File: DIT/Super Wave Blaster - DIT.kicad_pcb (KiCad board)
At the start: 2 copper layers, 28.2 x 21.2 mm, 20 parts, among them J1 SPDIF, J4 Power Input, U1 TLV73333PDBV, U2 DIT4096PW, U4 74LVC2G125

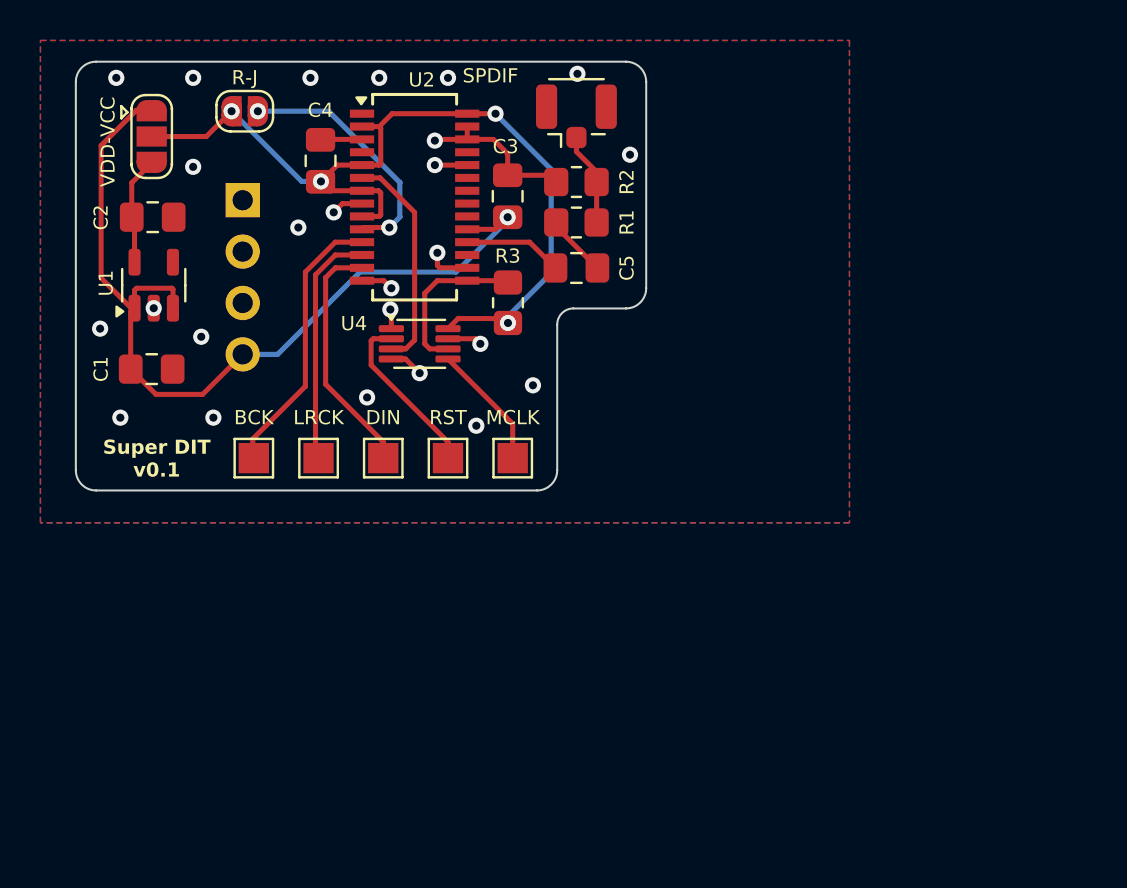
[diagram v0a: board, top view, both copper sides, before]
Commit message: DIT v0.2 - compact and right justified only
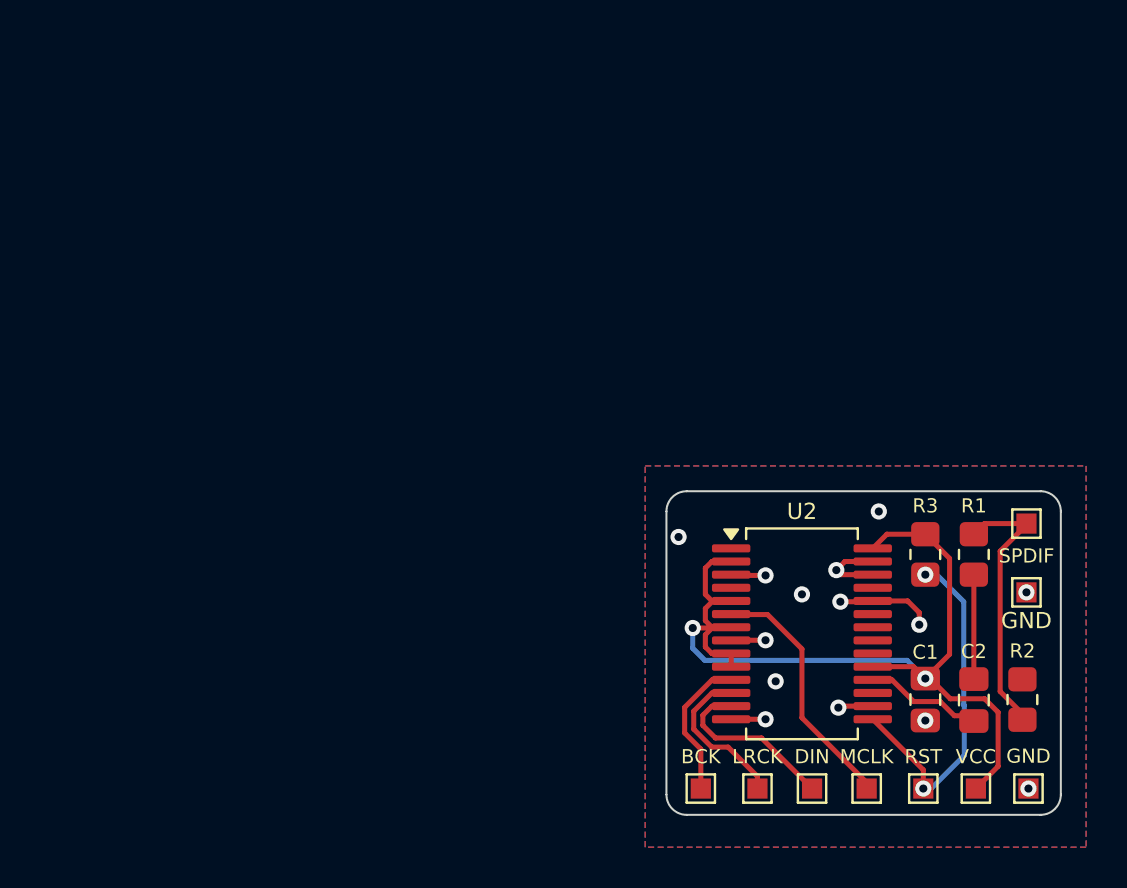
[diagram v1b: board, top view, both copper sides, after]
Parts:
- removed the C1 at (119.8, 79.0)
- removed the C2 at (119.8, 71.5)
- removed C4: 0.1uF, Capacitor_SMD:C_0805_2012Metric_Pad1.18x1.45mm_HandSolder
- removed J1: SPDIF, Connector_Coaxial:U.FL_Hirose_U.FL-R-SMT-1_Vertical
- removed J4: Power Input, Connector_PinHeader_2.54mm:PinHeader_1x04_P2.54mm_Vertical
- removed JP1: Jumper_3_Open, Jumper:SolderJumper-3_P1.3mm_Open_RoundedPad1.0x1.5mm
- removed JP2: R-J, Jumper:SolderJumper-2_P1.3mm_Open_RoundedPad1.0x1.5mm
- removed U1: TLV73333PDBV, Package_TO_SOT_SMD:SOT-23-5
- removed U4: 74LVC2G125, Package_SO:VSSOP-8_2.3x2mm_P0.5mm
- added TP6: SPDIF, TestPoint:TestPoint_Pad_1.0x1.0mm, F.Cu at (163.0, 86.6)
- added TP7: GND, TestPoint:TestPoint_Pad_1.0x1.0mm, F.Cu at (163.0, 90.0)
- added TP8: VCC, TestPoint:TestPoint_Pad_1.0x1.0mm, F.Cu at (160.5, 99.7)
- added TP9: GND, TestPoint:TestPoint_Pad_1.0x1.0mm, F.Cu at (163.1, 99.7)
- C1: renamed from C3; value 0.1uF -> 10uF
- R3: value 10k -> 470R
- TP1, TP2, TP3, TP4, TP5: footprint TestPoint:TestPoint_Pad_1.5x1.5mm -> TestPoint:TestPoint_Pad_1.0x1.0mm
- U2: footprint Package_SO:SSOP-28_3.9x9.9mm_P0.635mm -> Package_SO:SSOP-28_5.3x10.2mm_P0.65mm
- moved R2 33.8 mm to (162.8, 95.3), turned to -90 degrees
- moved C1 32.3 mm to (158.0, 95.3), turned to -90 degrees
- moved C2 29.0 mm to (160.4, 95.4), turned to -90 degrees
- moved U2 28.9 mm to (151.9, 92.1)
- moved TP5 28.6 mm to (157.9, 99.7)
- moved TP1 27.5 mm to (146.9, 99.7)
- moved TP2 27.2 mm to (149.7, 99.7)
- moved TP3 26.8 mm to (152.4, 99.7)
- moved R1 25.6 mm to (160.4, 88.2), turned to 90 degrees
- moved R3 24.1 mm to (158.0, 88.2), turned to 90 degrees
- moved TP4 23.9 mm to (155.1, 99.7)
- renumbered C5 to C2
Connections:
- R3 pad 1: RST_B -> RST
- R3 pad 2: VIO -> VCC
- U2 pad 10: FMT1 -> VCC
- U2 pad 15: RST_B -> RST
- U2 pad 2: VIO -> VCC
- U2 pad 28: VIO -> VCC
- U2 pad 5: VIO -> VCC
- U2 pad 6: MCLK_B -> MCLK
- U2 pad 7: VIO -> VCC
- U2 pad 9: VIO -> VCC
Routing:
- net VIO: track 44.1 -> 0.00 mm, vias 4 -> 0
- net FMT1: track 12.3 -> 0.00 mm, vias 2 -> 0
- net MCLK_B: track 10.9 -> 0.00 mm
- net Net-(R1-Pad2): track 4.61 -> 13.5 mm
- net RST: track 8.42 -> 17.2 mm, vias 0 -> 2
- net RST_B: track 8.16 -> 0.00 mm
- net GND: track 21.6 -> 14.4 mm, vias 25 -> 14
- net BCK: track 13.6 -> 7.21 mm
- net VDD: track 5.38 -> 0.00 mm
- net MCLK: track 6.23 -> 11.5 mm
- net LRCK: track 11.9 -> 7.83 mm
- net VCC: track 43.7 -> 47.3 mm, vias 1 -> 2
- net DIN: track 12.1 -> 8.78 mm
- net Net-(C2-Pad1): track 3.09 -> 5.16 mm
- net Net-(U2-TX+): track 4.89 -> 5.84 mm
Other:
- board size 28.2 x 21.2 mm -> 19.5 x 16 mm
- board text added: "Super DIT v0.2"
- board text removed: "Super DIT v0.1"
- board text removed: "VDD-VCC"

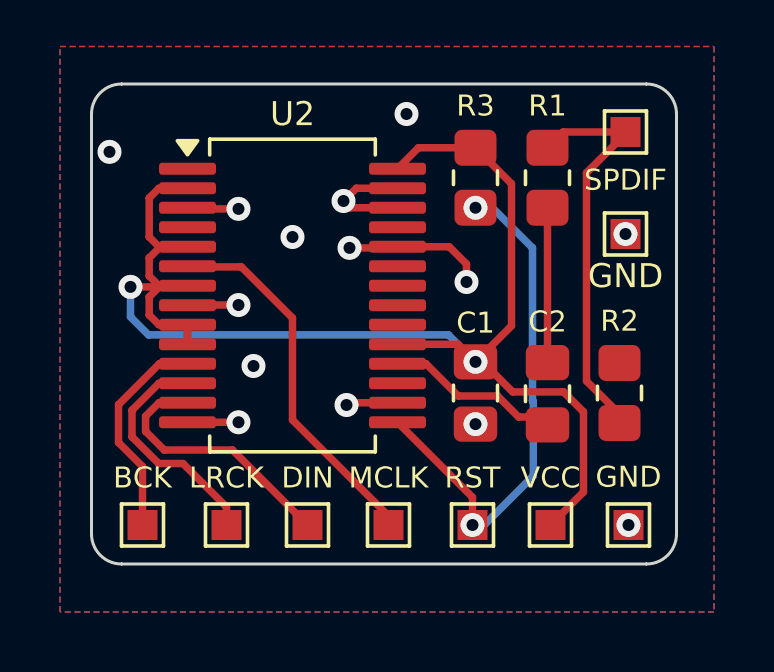
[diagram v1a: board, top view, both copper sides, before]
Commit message: DIT: Move vias off component pads
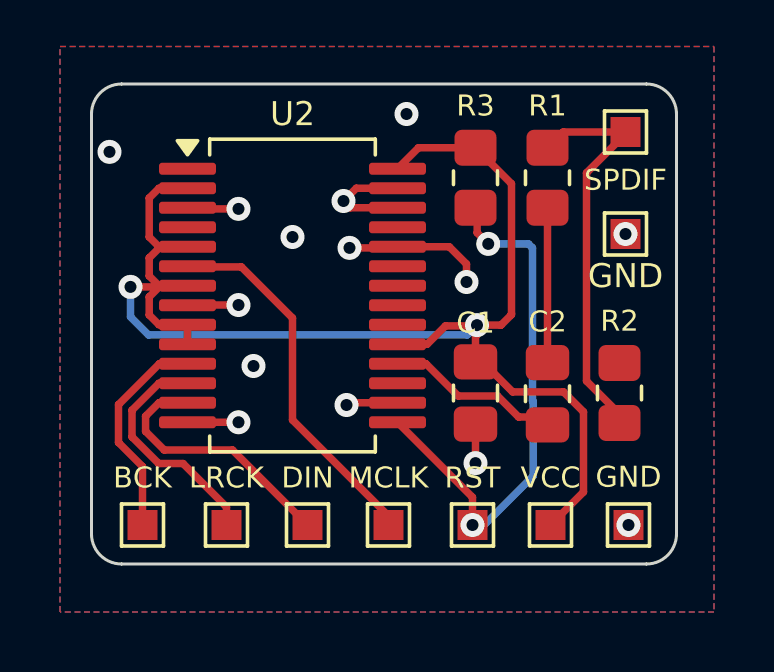
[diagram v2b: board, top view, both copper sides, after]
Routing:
- net GND: track 14.4 -> 15.7 mm
